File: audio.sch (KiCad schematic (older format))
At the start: 1 part, among them U1 DFR0299

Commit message: end of day save
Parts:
- added J?: Conn_01x02, Connector_JST:JST_XH_B2B-XH-A_1x02_P2.50mm_Vertical, symbol Connector_Generic:Conn_01x02
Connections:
- net 5V: now reaches U1.1 (VCC)
- net GND: now reaches U1.10 (GND), U1.7 (GND)
- net ESP2DFR: now reaches U1.2 (RX)
- net DFR2ESP: now reaches U1.3 (TX)
- net at U1.6 (SPK1): now also J?.2 (Pin_2)
- net at U1.8 (SPK2): now also J?.1 (Pin_1)
- no-connect marks 0 -> 5
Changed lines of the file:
@@
 	1    0    0    -1
 $EndComp
+$Comp
+L Connector_Generic:Conn_01x02 J?
+U 1 1 5FC6CA52
+P 4975 2850
+F 0 "J?" H 4893 2525 50  0000 C CNN
+F 1 "Conn_01x02" H 4893 2616 50  0000 C CNN
+F 2 "Connector_JST:JST_XH_B2B-XH-A_1x02_P2.50mm_Vertical" H 4975 2850 50  0001 C CNN
+F 3 "~" H 4975 2850 50  0001 C CNN
+	1    4975 2850
+	-1   0    0    1
+$EndComp
+Wire Wire Line
+	5175 2750 5525 2750
+Wire Wire Line
+	5175 2850 5525 2850
+Text GLabel 6925 3050 2    50   Input ~ 0
+GND
+Wire Wire Line
+	6725 3050 6925 3050
+Text GLabel 6875 1750 2    50   Input ~ 0
+5V
+Wire Wire Line
+	6725 1750 6875 1750
+NoConn ~ 6725 1950
+NoConn ~ 6725 2050
+Text GLabel 6850 2350 2    50   Input ~ 0
+ESP2DFR
+Text GLabel 6850 2250 2    50   Input ~ 0
+DFR2ESP
+Wire Wire Line
+	6725 2250 6850 2250
+Wire Wire Line
+	6725 2350 6850 2350
+NoConn ~ 5525 2150
+NoConn ~ 5525 1950
+NoConn ~ 5525 2250
 $EndSCHEMATC

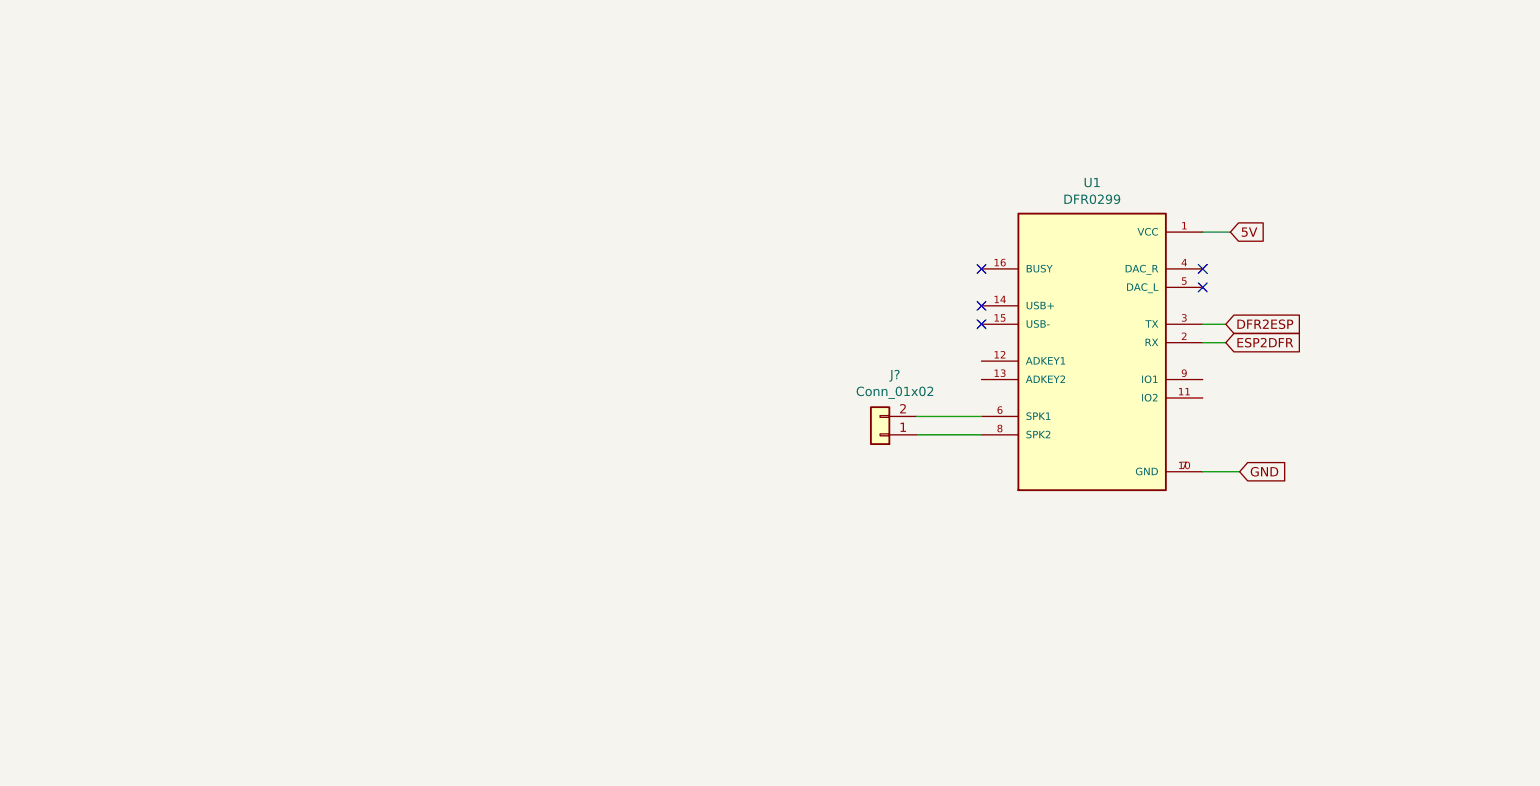
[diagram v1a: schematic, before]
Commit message: fin schéma, début placement
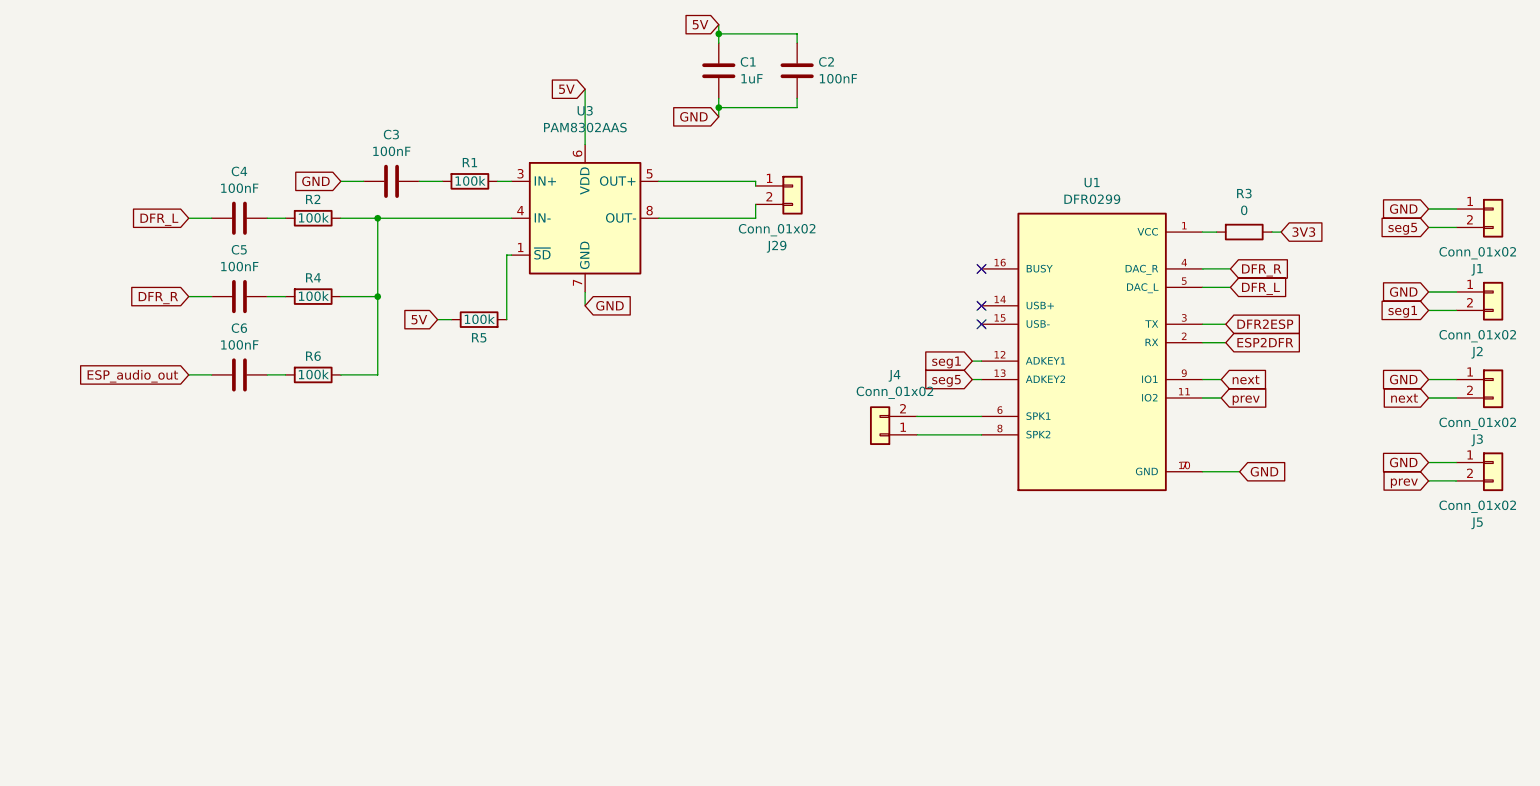
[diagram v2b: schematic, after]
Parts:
- added C1: 1uF, Capacitor_SMD:C_0603_1608Metric_Pad1.05x0.95mm_HandSolder, symbol Device:C
- added C2, C3, C4, C5, C6: 100nF, Capacitor_SMD:C_0603_1608Metric_Pad1.05x0.95mm_HandSolder, symbol Device:C
- added J1, J2, J29, J3, J5: Conn_01x02, Connector_JST:JST_XH_B2B-XH-A_1x02_P2.50mm_Vertical, symbol Connector_Generic:Conn_01x02
- added R1, R2, R4, R5, R6: 100k, Resistor_SMD:R_0603_1608Metric_Pad1.05x0.95mm_HandSolder, symbol Device:R
- added R3: 0, Resistor_SMD:R_0603_1608Metric_Pad1.05x0.95mm_HandSolder, symbol Device:R
- added U3: PAM8302AAS, Package_SO:MSOP-8_3x3mm_P0.65mm, symbol Amplifier_Audio:PAM8302AAS
- gave numbers to parts that had none: 1
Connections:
- net 5V: now also C1.2, C2.2, R5.1, U3.6 (VDD); no longer U1.1 (VCC)
- net GND: now also C1.1, C2.1, C3.2, J1.1 (Pin_1), J2.1 (Pin_1), J3.1 (Pin_1), J5.1 (Pin_1), U3.7 (GND)
- net prev: now reaches U1.11 (IO2)
- net prev: now also J5.2 (Pin_2)
- net seg1: now reaches U1.12 (ADKEY1)
- net seg1: now also J2.2 (Pin_2)
- net seg5: now reaches U1.13 (ADKEY2)
- net seg5: now also J1.2 (Pin_2)
- net DFR_R: now reaches U1.4 (DAC_R)
- net DFR_R: now also C5.2
- net DFR_L: now reaches U1.5 (DAC_L)
- net DFR_L: now also C4.2
- net next: now reaches U1.9 (IO1)
- net next: now also J3.2 (Pin_2)
- new net: R3.2, U1.1 (VCC)
- new net: R5.2, U3.1 (~SD)
- new net: R1.1, U3.3 (IN+)
- new net: R2.1, R4.1, R6.1, U3.4 (IN-)
- new net: J29.1 (Pin_1), U3.5 (OUT+)
- new net: J29.2 (Pin_2), U3.8 (OUT-)
- new net: C3.1, R1.2
- new net: C4.1, R2.2
- new net: C5.1, R4.2
- new net: C6.1, R6.2
- new net 3V3: R3.1
- new net ESP_audio_out: C6.2
- no-connect marks 5 -> 3

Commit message: simplifying + proper pins for uart + sd card host implemented
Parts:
- removed J1, J2, J3, J4, J5: Conn_01x02, Connector_JST:JST_XH_B2B-XH-A_1x02_P2.50mm_Vertical, symbol Connector_Generic:Conn_01x02
- removed R3: 0, Resistor_SMD:R_0603_1608Metric_Pad1.05x0.95mm_HandSolder, symbol Device:R
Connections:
- net 3V3: now also U1.1 (VCC)
- net ESP_audio_out renamed ESP_audio_out_div
- net next: no longer names the net of U1.9 (IO1)
- net prev: no longer names the net of U1.11 (IO2)
- net seg1: no longer names the net of U1.12 (ADKEY1)
- net seg5: no longer names the net of U1.13 (ADKEY2)
- no-connect marks 3 -> 9
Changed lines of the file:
@@
 	1    0    0    -1
 $EndComp
-$Comp
-L Connector_Generic:Conn_01x02 J4
-U 1 1 5FC6CA52
-P 4975 2850
-F 0 "J4" H 4893 2525 50  0000 C CNN
-F 1 "Conn_01x02" H 4893 2616 50  0000 C CNN
-F 2 "Connector_JST:JST_XH_B2B-XH-A_1x02_P2.50mm_Vertical" H 4975 2850 50  0001 C CNN
-F 3 "~" H 4975 2850 50  0001 C CNN
-	1    4975 2850
-	-1   0    0    1
-$EndComp
-Wire Wire Line
-	5175 2750 5525 2750
-Wire Wire Line
-	5175 2850 5525 2850
 Text GLabel 6925 3050 2    50   Input ~ 0
 GND
 Wire Wire Line
 	6725 3050 6925 3050
-Text GLabel 7150 1750 2    50   Input ~ 0
+Text GLabel 6800 1750 2    50   Input ~ 0
 3V3
 Text GLabel 6850 2350 2    50   Input ~ 0
@@
 NoConn ~ 5525 1950
 NoConn ~ 5525 2250
-$Comp
-L Connector_Generic:Conn_01x02 J1
-U 1 1 5FE05EE0
-P 8300 1625
-F 0 "J1" H 8218 1300 50  0000 C CNN
-F 1 "Conn_01x02" H 8218 1391 50  0000 C CNN
-F 2 "Connector_JST:JST_XH_B2B-XH-A_1x02_P2.50mm_Vertical" H 8300 1625 50  0001 C CNN
-F 3 "~" H 8300 1625 50  0001 C CNN
-	1    8300 1625
-	1    0    0    -1
-$EndComp
-Text GLabel 5475 2550 0    50   Input ~ 0
-seg5
-Text GLabel 5475 2450 0    50   Input ~ 0
-seg1
-Text GLabel 6825 2550 2    50   Input ~ 0
-next
-Text GLabel 6825 2650 2    50   Input ~ 0
-prev
-Wire Wire Line
-	6725 2550 6825 2550
-Wire Wire Line
-	6725 2650 6825 2650
-Wire Wire Line
-	5475 2450 5525 2450
-Wire Wire Line
-	5475 2550 5525 2550
-Text GLabel 7950 1725 0    50   Input ~ 0
-seg5
-Text GLabel 7950 2175 0    50   Input ~ 0
-seg1
-Text GLabel 7950 2650 0    50   Input ~ 0
-next
-Text GLabel 7950 3100 0    50   Input ~ 0
-prev
-Text GLabel 7950 1625 0    50   Input ~ 0
-GND
-Wire Wire Line
-	7950 1625 8100 1625
-Wire Wire Line
-	7950 1725 8100 1725
-$Comp
-L Connector_Generic:Conn_01x02 J2
-U 1 1 5FE089E1
-P 8300 2075
-F 0 "J2" H 8218 1750 50  0000 C CNN
-F 1 "Conn_01x02" H 8218 1841 50  0000 C CNN
-F 2 "Connector_JST:JST_XH_B2B-XH-A_1x02_P2.50mm_Vertical" H 8300 2075 50  0001 C CNN
-F 3 "~" H 8300 2075 50  0001 C CNN
-	1    8300 2075
-	1    0    0    -1
-$EndComp
-Text GLabel 7950 2075 0    50   Input ~ 0
-GND
-Wire Wire Line
-	7950 2075 8100 2075
-Wire Wire Line
-	7950 2175 8100 2175
-$Comp
-L Connector_Generic:Conn_01x02 J3
-U 1 1 5FE09440
-P 8300 2550
-F 0 "J3" H 8218 2225 50  0000 C CNN
-F 1 "Conn_01x02" H 8218 2316 50  0000 C CNN
-F 2 "Connector_JST:JST_XH_B2B-XH-A_1x02_P2.50mm_Vertical" H 8300 2550 50  0001 C CNN
-F 3 "~" H 8300 2550 50  0001 C CNN
-	1    8300 2550
-	1    0    0    -1
-$EndComp
-$Comp
-L Connector_Generic:Conn_01x02 J5
-U 1 1 5FE095FE
-P 8300 3000
-F 0 "J5" H 8218 2675 50  0000 C CNN
-F 1 "Conn_01x02" H 8218 2766 50  0000 C CNN
-F 2 "Connector_JST:JST_XH_B2B-XH-A_1x02_P2.50mm_Vertical" H 8300 3000 50  0001 C CNN
-F 3 "~" H 8300 3000 50  0001 C CNN
-	1    8300 3000
-	1    0    0    -1
-$EndComp
-Text GLabel 7950 2550 0    50   Input ~ 0
-GND
-Text GLabel 7950 3000 0    50   Input ~ 0
-GND
-Wire Wire Line
-	7950 2550 8100 2550
-Wire Wire Line
-	7950 2650 8100 2650
-Wire Wire Line
-	7950 3000 8100 3000
-Wire Wire Line
-	7950 3100 8100 3100
 Text GLabel 6875 1950 2    50   Input ~ 0
 DFR_R
@@
 Text GLabel 1225 1675 0    50   Input ~ 0
 DFR_L
-$Comp
-L Device:R R?
-U 1 1 5FE1321B
-P 6950 1750
-AR Path="/5FC6D1B4/5FE1321B" Ref="R?"  Part="1"
-AR Path="/5FC6C772/5FE1321B" Ref="R3"  Part="1"
-F 0 "R3" V 6743 1750 50  0000 C CNN
-F 1 "0" V 6834 1750 50  0000 C CNN
-F 2 "Resistor_SMD:R_0603_1608Metric_Pad1.05x0.95mm_HandSolder" V 6880 1750 50  0001 C CNN
-F 3 "~" H 6950 1750 50  0001 C CNN
-	1    6950 1750
-	0    1    1    0
-$EndComp
 Wire Wire Line
 	6725 1750 6800 1750
-Wire Wire Line
-	7100 1750 7150 1750
 Text GLabel 1225 2525 0    50   Input ~ 0
-ESP_audio_out
+ESP_audio_out_div
 $Comp
 L Amplifier_Audio:PAM8302AAS U3
@@
 Wire Wire Line
 	4300 1675 4300 1600
+NoConn ~ 5525 2750
+NoConn ~ 5525 2850
+NoConn ~ 6725 2550
+NoConn ~ 6725 2650
+NoConn ~ 5525 2450
+NoConn ~ 5525 2550
 $EndSCHEMATC

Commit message: maj
simplification dfr
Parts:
- removed U1: DFR0299, Chimere:MODULE_DFR0299, symbol Chimere:DFR0299
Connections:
- net DFR_L renamed DAC_Lout
- net DFR_R renamed DAC_Rout
- no-connect marks 9 -> 0
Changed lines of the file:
@@
 $Descr A4 11693 8268
 encoding utf-8
-Sheet 3 5
+Sheet 3 6
 Title ""
 Date ""
@@
 Comment4 ""
 $EndDescr
-$Comp
-L Chimere:DFR0299 U1
-U 1 1 5FC6C86F
-P 6125 2350
-F 0 "U1" H 6125 3217 50  0000 C CNN
-F 1 "DFR0299" H 6125 3126 50  0000 C CNN
-F 2 "Chimere:MODULE_DFR0299" H 6125 2350 50  0001 L BNN
-F 3 "" H 6125 2350 50  0001 L BNN
-F 4 "Dfplayer - a Mini Mp3 Player" H 6125 2350 50  0001 L BNN "DESCRIPTION"
-F 5 "DFRobot" H 6125 2350 50  0001 L BNN "MF"
-F 6 "Unavailable" H 6125 2350 50  0001 L BNN "AVAILABILITY"
-F 7 "None" H 6125 2350 50  0001 L BNN "PRICE"
-F 8 "DFR0299" H 6125 2350 50  0001 L BNN "MP"
-F 9 "None" H 6125 2350 50  0001 L BNN "PACKAGE"
-	1    6125 2350
-	1    0    0    -1
-$EndComp
-Text GLabel 6925 3050 2    50   Input ~ 0
-GND
-Wire Wire Line
-	6725 3050 6925 3050
-Text GLabel 6800 1750 2    50   Input ~ 0
-3V3
-Text GLabel 6850 2350 2    50   Input ~ 0
-ESP2DFR
-Text GLabel 6850 2250 2    50   Input ~ 0
-DFR2ESP
-Wire Wire Line
-	6725 2250 6850 2250
-Wire Wire Line
-	6725 2350 6850 2350
-NoConn ~ 5525 2150
-NoConn ~ 5525 1950
-NoConn ~ 5525 2250
-Text GLabel 6875 1950 2    50   Input ~ 0
-DFR_R
-Text GLabel 6875 2050 2    50   Input ~ 0
-DFR_L
-Wire Wire Line
-	6725 1950 6875 1950
-Wire Wire Line
-	6725 2050 6875 2050
-Text GLabel 1225 2100 0    50   Input ~ 0
-DFR_R
-Text GLabel 1225 1675 0    50   Input ~ 0
-DFR_L
-Wire Wire Line
-	6725 1750 6800 1750
 Text GLabel 1225 2525 0    50   Input ~ 0
 ESP_audio_out_div
@@
 Wire Wire Line
 	4300 1675 4300 1600
-NoConn ~ 5525 2750
-NoConn ~ 5525 2850
-NoConn ~ 6725 2550
-NoConn ~ 6725 2650
-NoConn ~ 5525 2450
-NoConn ~ 5525 2550
+Text GLabel 1225 1675 0    50   Input ~ 0
+DAC_Lout
+Text GLabel 1225 2100 0    50   Input ~ 0
+DAC_Rout
 $EndSCHEMATC

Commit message: modification audio + alim
utilisation du module Audio_Facile
+ utilisation d'un rotary switch rotary potentiometer
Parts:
- removed C1: 1uF, Capacitor_SMD:C_0603_1608Metric_Pad1.05x0.95mm_HandSolder, symbol Device:C
- removed C2, C3: 100nF, Capacitor_SMD:C_0603_1608Metric_Pad1.05x0.95mm_HandSolder, symbol Device:C
- removed R1: 100k, Resistor_SMD:R_0603_1608Metric_Pad1.05x0.95mm_HandSolder, symbol Device:R
- removed U3: PAM8302AAS, Package_SO:MSOP-8_3x3mm_P0.65mm, symbol Amplifier_Audio:PAM8302AAS
- added U1: Audio_Facile, Chimere:Audio_Facile, symbol Chimere:Audio_Facile
- added U3: rot_pot_rot_sw, Chimere:PTR901, symbol Chimere:rot_pot_rot_sw
- R2, R4, R6: value 100k -> 1k
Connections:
- net 5V: now also U1.2 (5V)
- net GND: now also U1.4 (GND), U3.3 (pot_1)
- net at R5.2: now also U1.3 (SD)
- net at R2.1, R4.1, R6.1: now also U3.5 (pot_3)
- net at J29.1 (Pin_1): now also U1.1 (OUT_P)
- net at J29.2 (Pin_2): now also U1.5 (OUT_N)
- new net: U1.6 (IN), U3.4 (pot_2)
- new net VBAT1: U3.2 (SW_2)
- new net VBAT2: U3.1 (SW_1)
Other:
- moved on the sheet: C4, C5, C6, J29, R2, R4, R5, R6
